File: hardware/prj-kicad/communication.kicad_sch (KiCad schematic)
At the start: 12 parts, among them P3 CONN_2x2, SW1 JUMPER, U2 SN65HVD72, U3 LTV814, U4 SN74LVC1G14

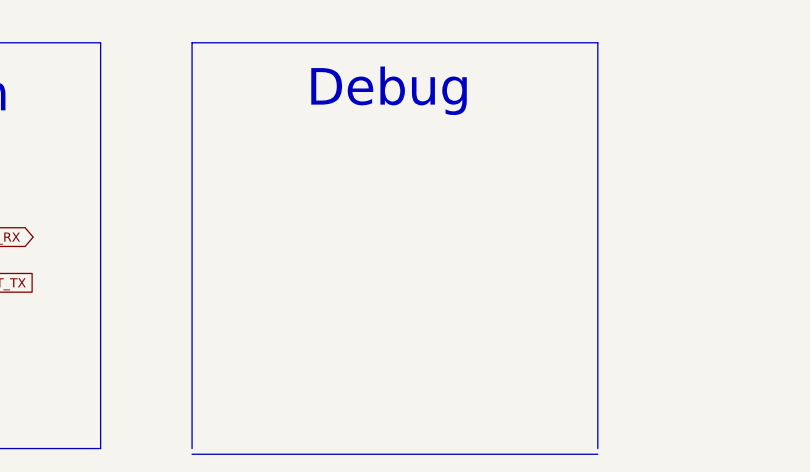
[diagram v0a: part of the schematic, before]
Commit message: Hardware: Finish current sensor interface and create production files for rev1
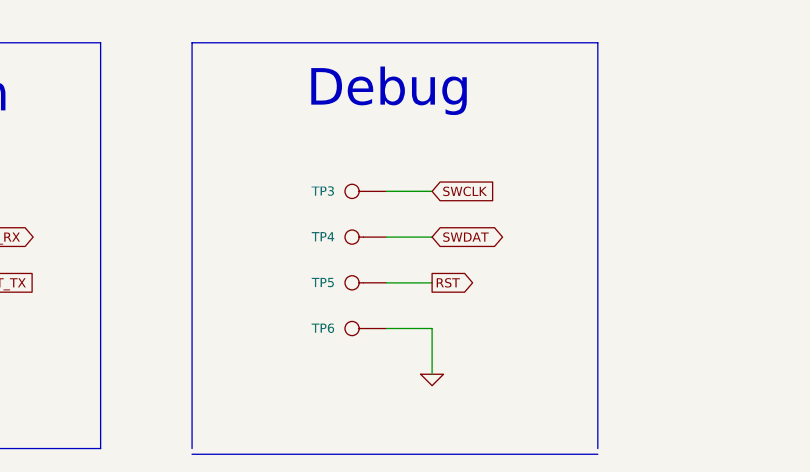
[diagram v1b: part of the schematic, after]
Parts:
- added TP3, TP4, TP5, TP6: CONN_1, cowdin-3a-pwrmon:TP_SMD, symbol cowdin-3a-pwrmon:CONN_1
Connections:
- net GND: now also TP6.1
- new net RST: TP5.1
- new net SWCLK: TP3.1
- new net SWDAT: TP4.1
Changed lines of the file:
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@@
+    (stroke (width 0) (type default) (color 0 0 0 0))
+  )
+  (wire (pts (xy 112.395 151.765) (xy 117.475 151.765))
     (stroke (width 0) (type default) (color 0 0 0 0))
   )
@@
     (stroke (width 0) (type default) (color 0 0 0 0))
   )
+  (wire (pts (xy 112.395 141.605) (xy 117.475 141.605))
+    (stroke (width 0) (type default) (color 0 0 0 0))
+  )
+  (wire (pts (xy 117.475 156.845) (xy 117.475 161.925))
+    (stroke (width 0) (type default) (color 0 0 0 0))
+  )
   (wire (pts (xy 48.26 141.605) (xy 48.26 146.685))
     (stroke (width 0) (type default) (color 0 0 0 0))
@@
   )
   (wire (pts (xy 100.965 71.755) (xy 103.505 71.755))
+    (stroke (width 0) (type default) (color 0 0 0 0))
+  )
+  (wire (pts (xy 112.395 156.845) (xy 117.475 156.845))
+    (stroke (width 0) (type default) (color 0 0 0 0))
+  )
+  (wire (pts (xy 112.395 146.685) (xy 117.475 146.685))
     (stroke (width 0) (type default) (color 0 0 0 0))
   )
@@
     )
   )
+  (global_label "SWCLK" (shape input) (at 117.475 141.605 0) (fields_autoplaced)
+    (effects (font (size 1.016 1.016)) (justify left))
+    (property "Intersheet References" "${INTERSHEET_REFS}" (id 0) (at 124.3886 141.5415 0)
+      (effects (font (size 1.016 1.016)) (justify left) hide)
+    )
+  )
   (global_label "EXT_TX" (shape input) (at 66.04 151.765 0) (fields_autoplaced)
     (effects (font (size 1.016 1.016)) (justify left))
@@
     )
   )
+  (global_label "SWDAT" (shape bidirectional) (at 117.475 146.685 0) (fields_autoplaced)
+    (effects (font (size 1.016 1.016)) (justify left))
+    (property "Intersheet References" "${INTERSHEET_REFS}" (id 0) (at 124.1951 146.6215 0)
+      (effects (font (size 1.016 1.016)) (justify left) hide)
+    )
+  )
+  (global_label "RST" (shape output) (at 117.475 151.765 0) (fields_autoplaced)
+    (effects (font (size 1.016 1.016)) (justify left))
+    (property "Intersheet References" "${INTERSHEET_REFS}" (id 0) (at 122.1631 151.7015 0)
+      (effects (font (size 1.016 1.016)) (justify left) hide)
+    )
+  )
   (global_label "RS485_TX" (shape input) (at 187.325 64.135 180) (fields_autoplaced)
     (effects (font (size 1.27 1.27)) (justify right))
@@
     (pin "3")
     (pin "4")
+  )
+  (symbol (lib_id "cowdin-3a-pwrmon:CONN_1") (at 108.585 141.605 180) (unit 1)
+    (in_bom yes) (on_board yes)
+    (property "Reference" "TP3" (id 0) (at 106.68 141.605 0)
+      (effects (font (size 1.016 1.016)) (justify left))
+    )
+    (property "Value" "CONN_1" (id 1) (at 108.585 143.002 0)
+      (effects (font (size 0.762 0.762)) hide)
+    )
+    (property "Footprint" "cowdin-3a-pwrmon:TP_SMD" (id 2) (at 108.585 141.605 0)
+      (effects (font (size 1.524 1.524)) hide)
+    )
+    (property "Datasheet" "" (id 3) (at 108.585 141.605 0)
+      (effects (font (size 1.524 1.524)))
+    )
+    (pin "1")
   )
   (symbol (lib_id "cowdin-3a-pwrmon:GND") (at 70.485 74.295 0) (unit 1)
@@
     (pin "1")
   )
+  (symbol (lib_id "cowdin-3a-pwrmon:CONN_1") (at 108.585 151.765 180) (unit 1)
+    (in_bom yes) (on_board yes)
+    (property "Reference" "TP5" (id 0) (at 106.68 151.765 0)
+      (effects (font (size 1.016 1.016)) (justify left))
+    )
+    (property "Value" "CONN_1" (id 1) (at 108.585 153.162 0)
+      (effects (font (size 0.762 0.762)) hide)
+    )
+    (property "Footprint" "cowdin-3a-pwrmon:TP_SMD" (id 2) (at 108.585 151.765 0)
+      (effects (font (size 1.524 1.524)) hide)
+    )
+    (property "Datasheet" "" (id 3) (at 108.585 151.765 0)
+      (effects (font (size 1.524 1.524)))
+    )
+    (pin "1")
+  )
+  (symbol (lib_id "cowdin-3a-pwrmon:CONN_1") (at 108.585 146.685 180) (unit 1)
+    (in_bom yes) (on_board yes)
+    (property "Reference" "TP4" (id 0) (at 106.68 146.685 0)
+      (effects (font (size 1.016 1.016)) (justify left))
+    )
+    (property "Value" "CONN_1" (id 1) (at 108.585 148.082 0)
+      (effects (font (size 0.762 0.762)) hide)
+    )
+    (property "Footprint" "cowdin-3a-pwrmon:TP_SMD" (id 2) (at 108.585 146.685 0)
+      (effects (font (size 1.524 1.524)) hide)
+    )
+    (property "Datasheet" "" (id 3) (at 108.585 146.685 0)
+      (effects (font (size 1.524 1.524)))
+    )
+    (pin "1")
+  )
   (symbol (lib_id "cowdin-3a-pwrmon:GND") (at 57.15 96.52 0) (unit 1)
     (in_bom yes) (on_board yes) (fields_autoplaced)
@@
     (pin "5")
   )
+  (symbol (lib_id "cowdin-3a-pwrmon:CONN_1") (at 108.585 156.845 180) (unit 1)
+    (in_bom yes) (on_board yes)
+    (property "Reference" "TP6" (id 0) (at 106.68 156.845 0)
+      (effects (font (size 1.016 1.016)) (justify left))
+    )
+    (property "Value" "CONN_1" (id 1) (at 108.585 158.242 0)
+      (effects (font (size 0.762 0.762)) hide)
+    )
+    (property "Footprint" "cowdin-3a-pwrmon:TP_SMD" (id 2) (at 108.585 156.845 0)
+      (effects (font (size 1.524 1.524)) hide)
+    )
+    (property "Datasheet" "" (id 3) (at 108.585 156.845 0)
+      (effects (font (size 1.524 1.524)))
+    )
+    (pin "1")
+  )
   (symbol (lib_id "cowdin-3a-pwrmon:R") (at 109.855 71.755 90) (unit 1)
     (in_bom yes) (on_board yes)
@@
       (effects (font (size 1.524 1.524)))
     )
+    (pin "1")
+  )
+  (symbol (lib_id "cowdin-3a-pwrmon:GND") (at 117.475 161.925 0) (unit 1)
+    (in_bom yes) (on_board yes) (fields_autoplaced)
+    (property "Reference" "#PWR0173" (id 0) (at 117.475 161.925 0)
+      (effects (font (size 0.762 0.762)) hide)
+    )
+    (property "Value" "GND" (id 1) (at 117.475 163.703 0)
+      (effects (font (size 0.762 0.762)) hide)
+    )
+    (property "Footprint" "" (id 2) (at 117.475 161.925 0)
+      (effects (font (size 1.524 1.524)))
+    )
+    (property "Datasheet" "" (id 3) (at 117.475 161.925 0)
+      (effects (font (size 1.524 1.524)))
+    )
